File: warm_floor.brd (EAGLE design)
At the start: 100 x 80 mm, 30 parts, among them K1 G2R, Q1 BSS123, T1 BC847, T2 BC847, T3 BC847, X1 53047-04, X3 DG3XX-03-3.5, X4 DG3XX-02-3.5

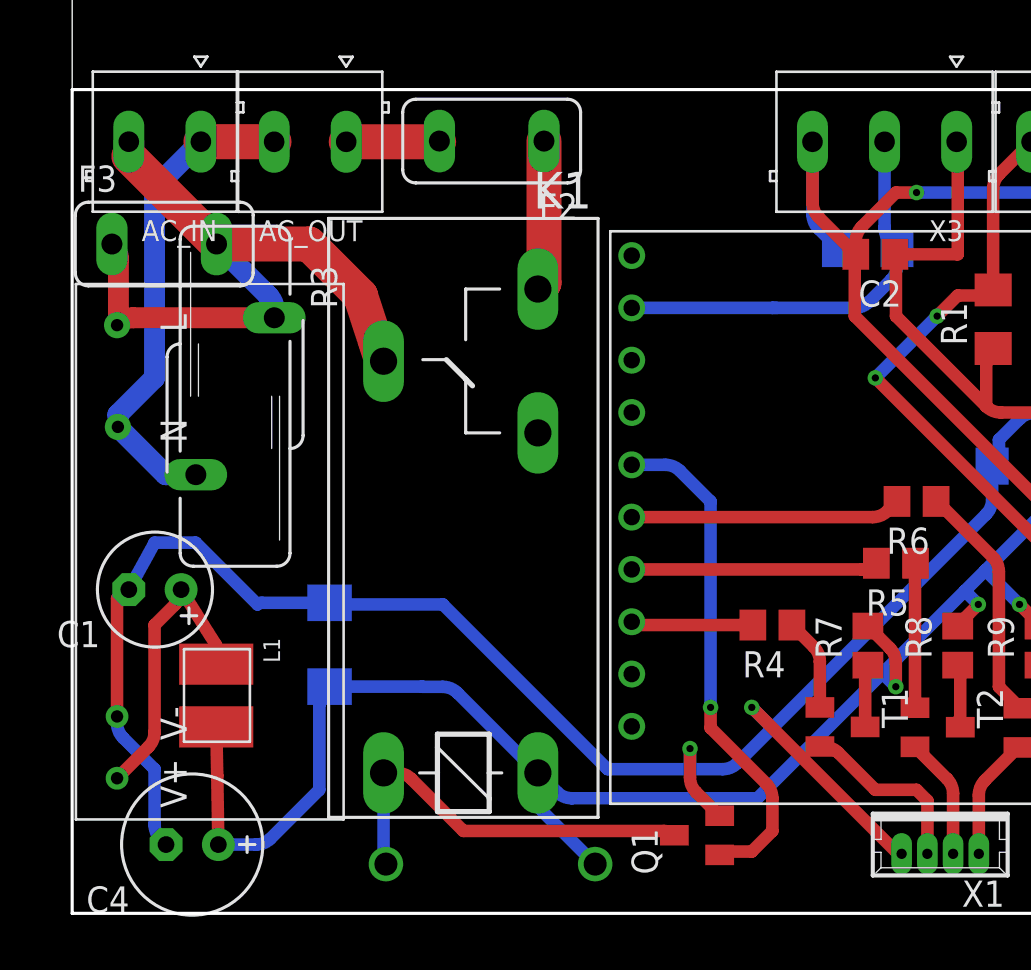
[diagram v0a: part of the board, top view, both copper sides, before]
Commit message: linked all wires
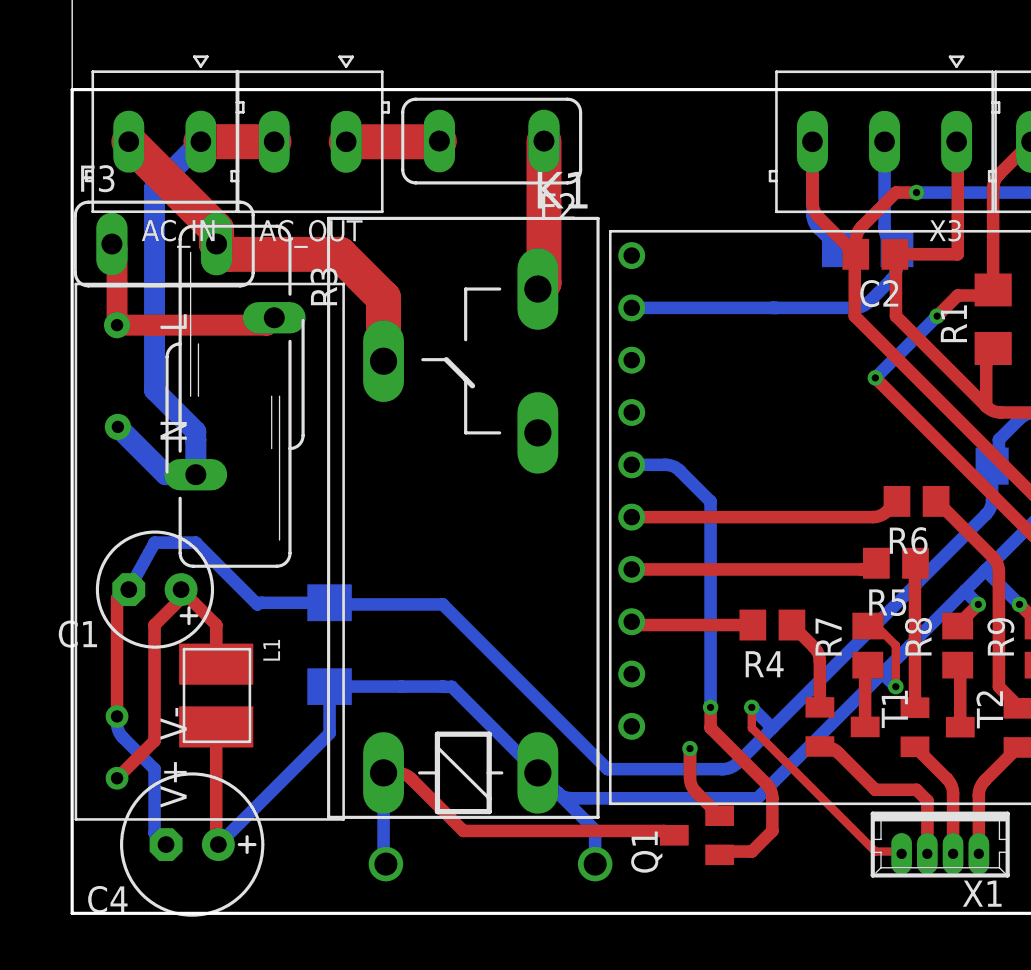
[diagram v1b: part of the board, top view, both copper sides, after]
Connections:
- new net N$1: C1.+, L1.P$1, U$2.V+
- new net N$2: F3.1, R3.1, U$2.L
- new net N$3: F2.1, K1.S
- new net N$5: AC_OUT.1, F2.2
- net L: no longer AC_OUT.1, F2.1, F2.2, F3.1, K1.S, R3.1, U$2.L
- net VCC: no longer C1.+, L1.P$1, U$2.V+
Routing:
- net L: track 46.2 -> 19.0 mm
- net VCC: track 94.7 -> 78.3 mm
- net N$1: track 0.00 -> 14.8 mm
- net N$2: track 0.00 -> 11.8 mm
- net N$3: track 0.00 -> 7.31 mm
- net N$5: track 0.00 -> 4.54 mm
- net N: track 23.8 -> 26.2 mm
- net GND: track 118.2 -> 118.8 mm

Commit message: Add files via upload
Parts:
- removed R3: S14K320, varistor:S14K320
- added F1: (no value), fuse:TR5
- added R10: S10K385, varistor:S10K385
- moved U$2 12.2 mm to (1.00, 27.0)
- moved F3 7.64 mm to (3.00, 25.0), turned to 270 degrees
- moved C1 3.40 mm to (3.65, 12.3)
- moved L1 1.41 mm to (8.63, 9.83)
- moved C4 1.00 mm to (6.83, 3.34)
- moved D1 0.38 mm to (20.3, 2.01)
- moved F2 0.36 mm to (20.1, 37.2)
- moved K1 0.25 mm to (18.9, 9.11)
- moved AC_OUT 0.13 mm to (11.6, 37.3)
- moved X3 0.13 mm to (39.4, 37.3)
- moved X4 0.13 mm to (48.3, 37.3)
- moved AC_IN 0.13 mm to (4.50, 37.3)
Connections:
- net N$3 renamed RELAY_OUT
- net N$5 renamed WF_L
- new net PS_L: F1.1, F3.1, U$2.L
- net L: now also F1.2; no longer F3.2
- net N: now also R10.2; no longer R3.2
- net N$2: now also F3.2, R10.1; no longer F3.1, R3.1, U$2.L
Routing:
- net PS_L: track 0.00 -> 8.78 mm
- net L: track 19.0 -> 24.2 mm
- net GND: track 118.8 -> 115.4 mm
- net N$2: track 11.8 -> 10.3 mm
- net VCC: track 78.3 -> 77.0 mm
- net N$1: track 14.8 -> 15.5 mm
- net N$4: track 19.7 -> 20.2 mm
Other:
- board size 100 x 80 mm -> 52 x 40 mm

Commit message: Last G2R version
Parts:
- removed AC_IN, AC_OUT: DG3XX-02-3.5, degson:DG350-3.5-02P
- added X5, X6: DG3XX-025.0, degson:DG300-5.0-02P
- D1: value 1N4004 -> (none); device diode:DO41-10 -> diode:SOD123
- D2: value SMBJ20A -> SMBJ15A
- F1: value (none) -> FUSETE5; device fuse:TR5 -> fuse:TE5
- R2: device resistor:R1206 -> rcl:R0805
- moved F2 5.02 mm to (25.1, 37.4)
- moved R5 2.55 mm to (37.5, 16.5)
- moved R2 2.48 mm to (36.3, 31.4), flipped to the top, turned to 90 degrees
- moved C3 2.05 mm to (47.7, 22.9), flipped to the top, turned to 270 degrees
- moved C2 2.00 mm to (39.0, 34.0), flipped to the bottom, turned to 0 degrees
- moved R4 1.77 mm to (32.7, 15.3)
- moved D1 1.62 mm to (18.8, 1.35)
- moved K1 1.49 mm to (18.9, 7.61)
- moved L1 1.41 mm to (9.63, 10.8)
- moved F1 1.13 mm to (5.00, 30.6)
- moved R6 1.00 mm to (41.0, 19.0)
- moved X1 0.63 mm to (42.1, 2.71)
- moved R1 0.58 mm to (44.9, 28.3), flipped to the bottom, turned to 0 degrees
- moved T3 0.50 mm to (46.5, 9.01)
- moved C4 0.39 mm to (6.96, 3.71)
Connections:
- net L: now also X5.2; no longer AC_IN.2
- net N: now also X5.1, X6.2; no longer AC_IN.1, AC_OUT.2
- net WF_L: now also X6.1; no longer AC_OUT.1
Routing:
- net GND: track 115.4 -> 2.31 mm, vias 2 -> 22
- net 3.3V: track 47.5 -> 41.7 mm, vias 1 -> 0
- net RELAY_OUT: track 7.19 -> 11.6 mm
- net L: track 24.2 -> 28.2 mm
- net NTC: track 34.1 -> 30.1 mm, vias 2 -> 1
- net N$19: track 4.50 -> 7.32 mm
- net N$16: track 12.0 -> 9.44 mm
- net N: track 26.1 -> 28.6 mm
- net N$20: track 7.02 -> 8.96 mm
- net DATA: track 19.9 -> 18.4 mm
- net N$1: track 15.5 -> 14.4 mm
- net RELAY: track 24.7 -> 23.6 mm
- net N$22: track 5.91 -> 5.03 mm
- net PS_L: track 8.78 -> 7.99 mm
- net N$21: track 11.6 -> 10.9 mm, vias 0 -> 2
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- added copper zone on layer 1, net GND
- added copper zone on layer 16, net GND
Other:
- outline, holes or cut-outs redrawn

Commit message: Pre-publish commit
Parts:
- removed X6: DG3XX-025.0, degson:DG300-5.0-02P
- added C5: 10u, rcl:E2,5-6
- added D3: (no value), diode:SMBJ
- added X2: DG3XX-025.0, degson:DG300-5.0-02P
- C3: device rcl:C1206 -> rcl:C0805
- K1: value G2R -> G5Q-1A; device relay:G2R -> relay:G5Q-1A
- R1: device resistor:R1206 -> rcl:R0805
- X3: value DG3XX-03-3.5 -> DG3XX-025.0; device degson:DG350-3.5-03P -> degson:DG300-5.0-02P
- X4: value DG3XX-02-3.5 -> DG3XX-03-3.5; device degson:DG350-3.5-02P -> degson:DG350-3.5-03P
- X5: value DG3XX-025.0 -> DG3XX-02-3.5; device degson:DG300-5.0-02P -> degson:DG350-3.5-02P
- moved X5 43.2 mm to (48.3, 37.3)
- moved X3 24.3 mm to (15.1, 37.5)
- moved U$2 14.2 mm to (7.36, 14.3)
- moved Q1 12.4 mm to (22.8, 13.7), flipped to the bottom, turned to 180 degrees
- moved F2 10.8 mm to (16.6, 30.8)
- moved K1 9.65 mm to (19.4, 17.3), turned to 270 degrees
- moved X4 8.89 mm to (39.4, 37.3)
- moved D1 7.19 mm to (18.4, 8.53), turned to 90 degrees
- moved D2 7.08 mm to (12.5, 5.96), turned to 270 degrees
- moved C2 2.24 mm to (37.0, 33.0)
- moved C4 1.16 mm to (8.04, 3.29), turned to 0 degrees
- moved R1 0.89 mm to (44.0, 28.0)
- moved C3 0.29 mm to (48.0, 23.0)
- flipped F1 to the top, turned to 180 degrees
- renumbered R10 to R3
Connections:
- removed net RELAY_OUT: F2.1, K1.S
- removed net WF_L: F2.2, X6.1
- new net N$5: F2.1, K1.2
- new net N$6: K1.3, X3.1
- new net N$7: D1.A, D3.A
- net 3.3V: now also X4.3, X5.1; no longer X3.3, X4.1
- net DATA: now also X4.2; no longer X3.2
- net GND: now also C5.-, X4.1; no longer X3.1
- net L: now also F2.2, X2.2; no longer K1.P, X5.2
- net N: now also X2.1, X3.2; no longer X5.1, X6.2
- net N$4: now also D3.C, K1.1; no longer D1.A, K1.2
- net NTC: now also X5.2; no longer X4.2
- net VCC: now also C5.+, K1.5; no longer K1.1
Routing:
- net N$6: track 0.00 -> 14.1 mm
- net N$4: track 20.8 -> 7.03 mm
- net RELAY: track 23.6 -> 10.1 mm, vias 1 -> 0
- net N$5: track 0.00 -> 12.7 mm
- net RELAY_OUT: track 11.6 -> 0.00 mm
- net L: track 28.2 -> 22.5 mm, vias 0 -> 1
- net WF_L: track 5.01 -> 0.00 mm
- net N$7: track 0.00 -> 4.33 mm
- net VCC: track 77.6 -> 75.2 mm, vias 2 -> 0
- net 3.3V: track 41.7 -> 42.8 mm
- net N: track 28.6 -> 27.9 mm
- net N$19: track 7.32 -> 7.53 mm, vias 0 -> 2
- net GND: track 2.31 -> 2.18 mm, vias 22 -> 36
- net N$20: track 8.96 -> 9.03 mm, vias 0 -> 2
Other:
- outline, holes or cut-outs redrawn
- board text added: "3.3V"
- board text added: "DATA"
- board text added: "GND"
- board text added: "L"
- board text added: "L_OUT"
- board text added: "N"
- board text added: "NTC"
- board text added: "V+"
- board text added: "Warm Floor Module v1"
- board text added: "panikena ©2018"
